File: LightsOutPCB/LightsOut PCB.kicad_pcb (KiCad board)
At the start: 2 copper layers, 68.6 x 53.3 mm, 8 parts, among them J1 Power, J2 Digital/PWM, J3 Analog, J4 Digital/PWM

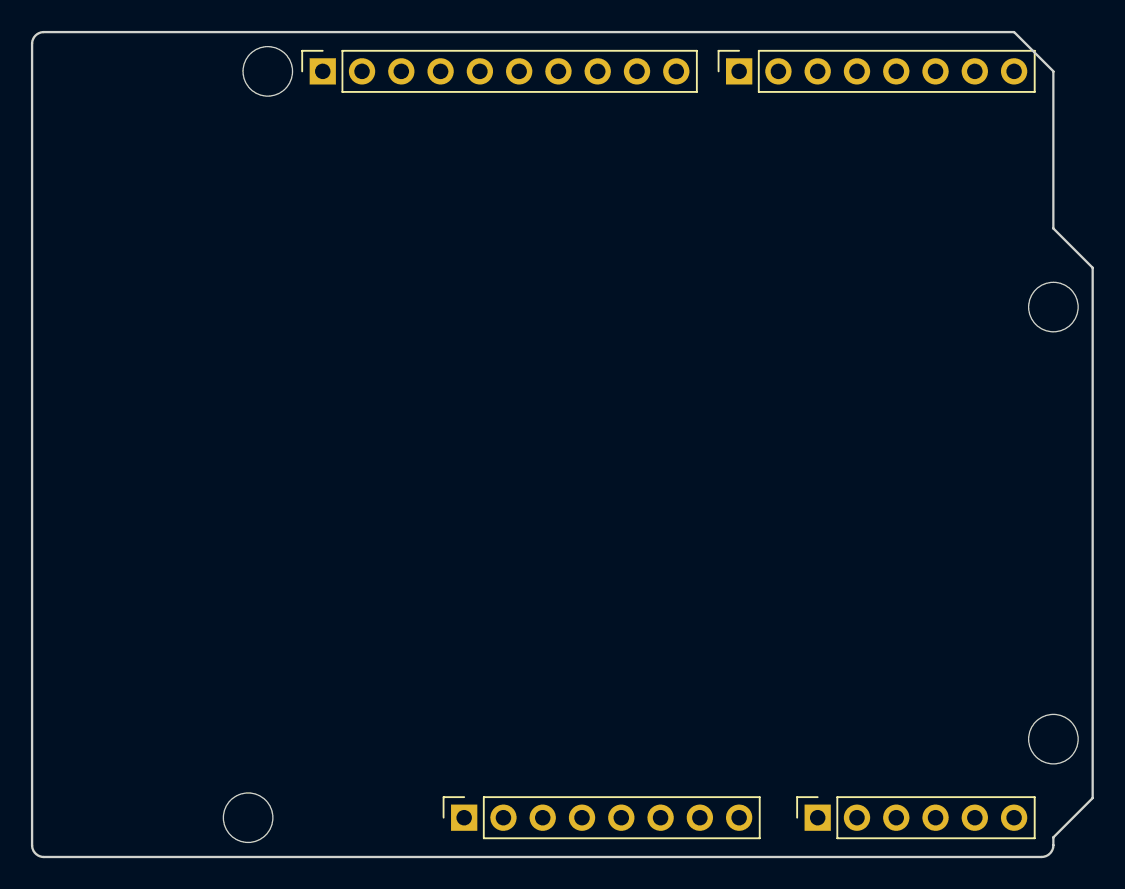
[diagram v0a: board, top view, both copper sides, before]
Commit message: finished initial placement
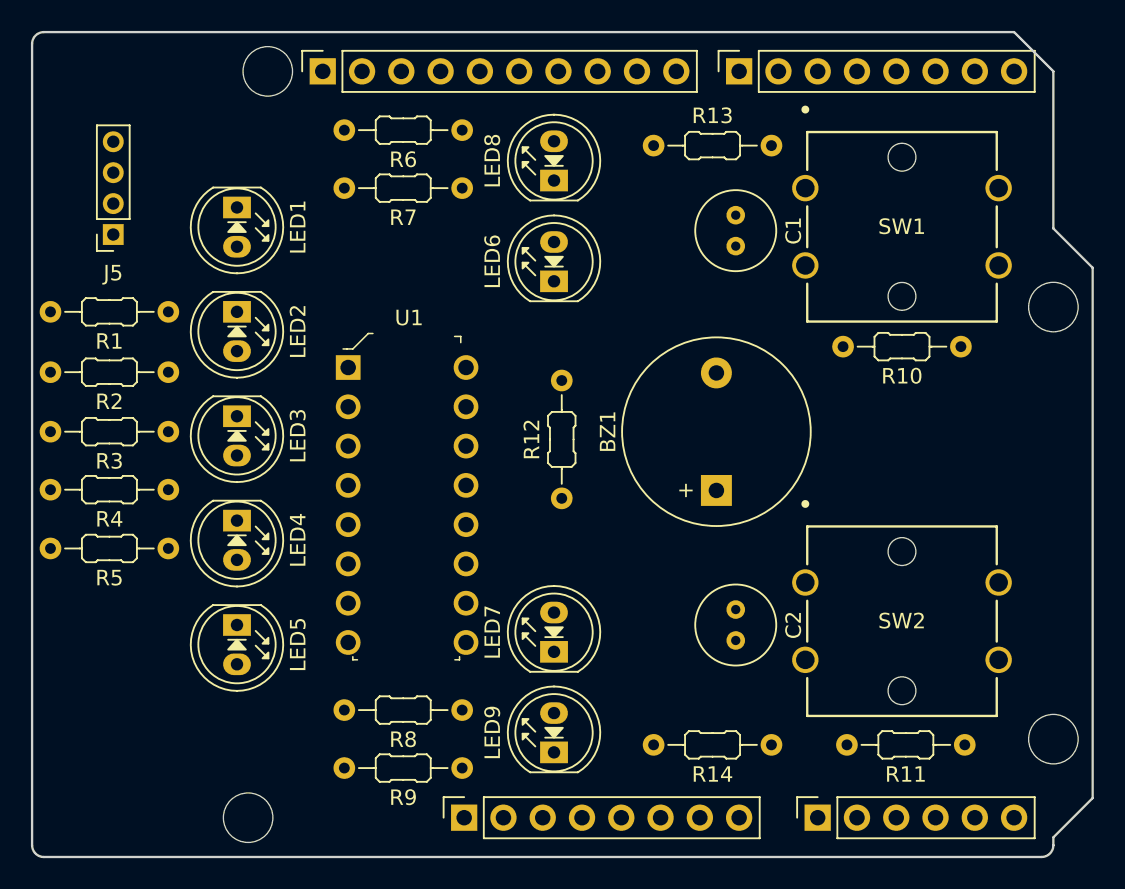
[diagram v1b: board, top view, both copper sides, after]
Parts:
- added BZ1: Buzzer, Buzzer_Beeper:MagneticBuzzer_StarMicronics_TMB, F.Cu at (144.2, 76.3)
- added C1: 0.1 uF, Capacitor_THT_AKL:C_Radial_D5.0mm_H7.0mm_P2.00mm, F.Cu at (145.5, 58.5)
- added C2: 0.1 uF, Capacitor_THT_AKL:C_Radial_D5.0mm_H7.0mm_P2.00mm, F.Cu at (145.5, 84.0)
- added J5: Conn_01x04_Pin, Connector_PinSocket_2.00mm:PinSocket_1x04_P2.00mm_Vertical, F.Cu at (105.2, 59.8)
- added LED1: LED_5mm_Red, LED_THT_AKL_Double:LED_D5.0mm, F.Cu at (113.2, 58.0)
- added LED2: LED_5mm_Red, LED_THT_AKL_Double:LED_D5.0mm, F.Cu at (113.2, 64.8)
- added LED3: LED_5mm_Red, LED_THT_AKL_Double:LED_D5.0mm, F.Cu at (113.2, 71.5)
- added LED4: LED_5mm_Red, LED_THT_AKL_Double:LED_D5.0mm, F.Cu at (113.2, 78.2)
- added LED5: LED_5mm_Red, LED_THT_AKL_Double:LED_D5.0mm, F.Cu at (113.2, 85.0)
- added LED6: LED_5mm_Yellow, LED_THT_AKL_Double:LED_D5.0mm, F.Cu at (133.8, 62.8)
- added LED7: LED_5mm_Yellow, LED_THT_AKL_Double:LED_D5.0mm, F.Cu at (133.8, 86.7)
- added LED8: LED_5mm_Green, LED_THT_AKL_Double:LED_D5.0mm, F.Cu at (133.8, 56.3)
- added LED9: LED_5mm_Green, LED_THT_AKL_Double:LED_D5.0mm, F.Cu at (133.8, 93.2)
- added R1: 330 Ω, Resistor_THT_AKL:R_Axial_DIN0204_L3.6mm_D1.6mm_P7.62mm_Horizontal, F.Cu at (108.8, 64.8)
- added R10: 10 kΩ, Resistor_THT_AKL:R_Axial_DIN0204_L3.6mm_D1.6mm_P7.62mm_Horizontal, F.Cu at (160.1, 67.0)
- added R11: 10 kΩ, Resistor_THT_AKL:R_Axial_DIN0204_L3.6mm_D1.6mm_P7.62mm_Horizontal, F.Cu at (160.3, 92.8)
- added R12: 560 Ω, Resistor_THT_AKL:R_Axial_DIN0204_L3.6mm_D1.6mm_P7.62mm_Horizontal, F.Cu at (134.2, 76.8)
- added R13: 100 Ω, Resistor_THT_AKL:R_Axial_DIN0204_L3.6mm_D1.6mm_P7.62mm_Horizontal, F.Cu at (140.2, 54.0)
- added R14: 100 Ω, Resistor_THT_AKL:R_Axial_DIN0204_L3.6mm_D1.6mm_P7.62mm_Horizontal, F.Cu at (147.8, 92.8)
- added R2: 330 Ω, Resistor_THT_AKL:R_Axial_DIN0204_L3.6mm_D1.6mm_P7.62mm_Horizontal, F.Cu at (108.8, 68.7)
- added R3: 330 Ω, Resistor_THT_AKL:R_Axial_DIN0204_L3.6mm_D1.6mm_P7.62mm_Horizontal, F.Cu at (108.8, 72.5)
- added R4: 330 Ω, Resistor_THT_AKL:R_Axial_DIN0204_L3.6mm_D1.6mm_P7.62mm_Horizontal, F.Cu at (108.8, 76.2)
- added R5: 330 Ω, Resistor_THT_AKL:R_Axial_DIN0204_L3.6mm_D1.6mm_P7.62mm_Horizontal, F.Cu at (108.8, 80.0)
- added R6: 220 Ω, Resistor_THT_AKL:R_Axial_DIN0204_L3.6mm_D1.6mm_P7.62mm_Horizontal, F.Cu at (127.8, 53.0)
- added R7: 220 Ω, Resistor_THT_AKL:R_Axial_DIN0204_L3.6mm_D1.6mm_P7.62mm_Horizontal, F.Cu at (127.8, 56.8)
- added R8: 220 Ω, Resistor_THT_AKL:R_Axial_DIN0204_L3.6mm_D1.6mm_P7.62mm_Horizontal, F.Cu at (127.8, 90.5)
- added R9: 220 Ω, Resistor_THT_AKL:R_Axial_DIN0204_L3.6mm_D1.6mm_P7.62mm_Horizontal, F.Cu at (127.8, 94.2)
- added SW1: B3W-4050, push-button-switch:SW_B3W-4050_OMR, F.Cu at (150.0, 56.8)
- added SW2: B3W-4050, push-button-switch:SW_B3W-4050_OMR, F.Cu at (150.0, 82.3)
- added U1: SN74HC595N, digikey-footprints:DIP-16_W7.62mm, F.Cu at (120.4, 68.3)
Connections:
- net +3V3 renamed /+3.3V
- net VCC renamed /Vin
- J2 pad 1: /SCL/A5 -> /SCL
- J2 pad 2: /SDA/A4 -> /SDA
- J2 pad 7: /*11 -> /11
- J2 pad 8: /*10 -> /10
- J2 pad 9: /*9 -> /9
- J3 pad 5: /SDA/A4 -> /A4
- J3 pad 6: /SCL/A5 -> /A5
- J4 pad 2: /*6 -> /6
- J4 pad 3: /*5 -> /5
- J4 pad 5: /*3 -> /3
